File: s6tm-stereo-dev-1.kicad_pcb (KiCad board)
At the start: 4 copper layers, 184 parts, among them J1 Micro_SD_Card_Det1, J2 Conn_01x04_Pin, J3 USB_C_Receptacle_USB2.0_14P, J4 Conn_01x02, J5 AudioJack4, J6 Conn_01x02, J7 Conn_01x02, J8 Conn_01x02, Q1 Q_NMOS, Q2 Q_NMOS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

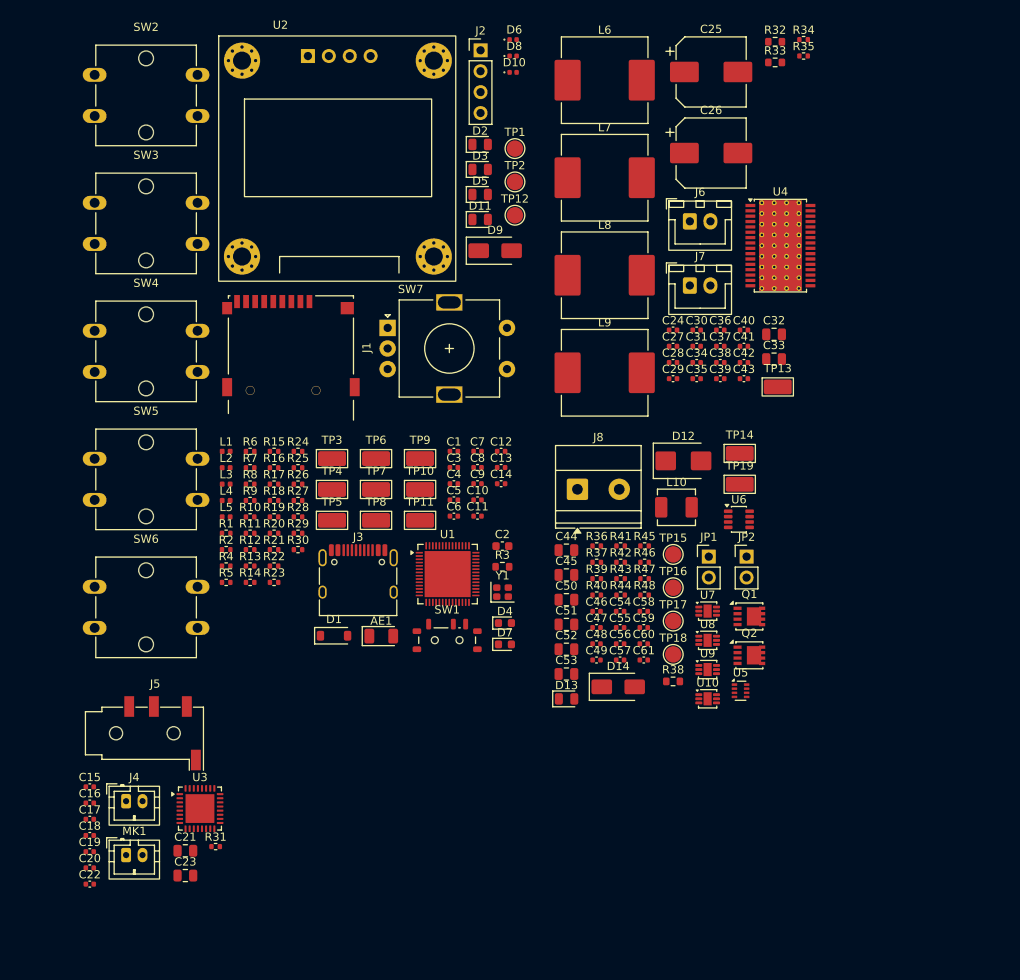
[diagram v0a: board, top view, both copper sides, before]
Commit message: pcb: initial layout
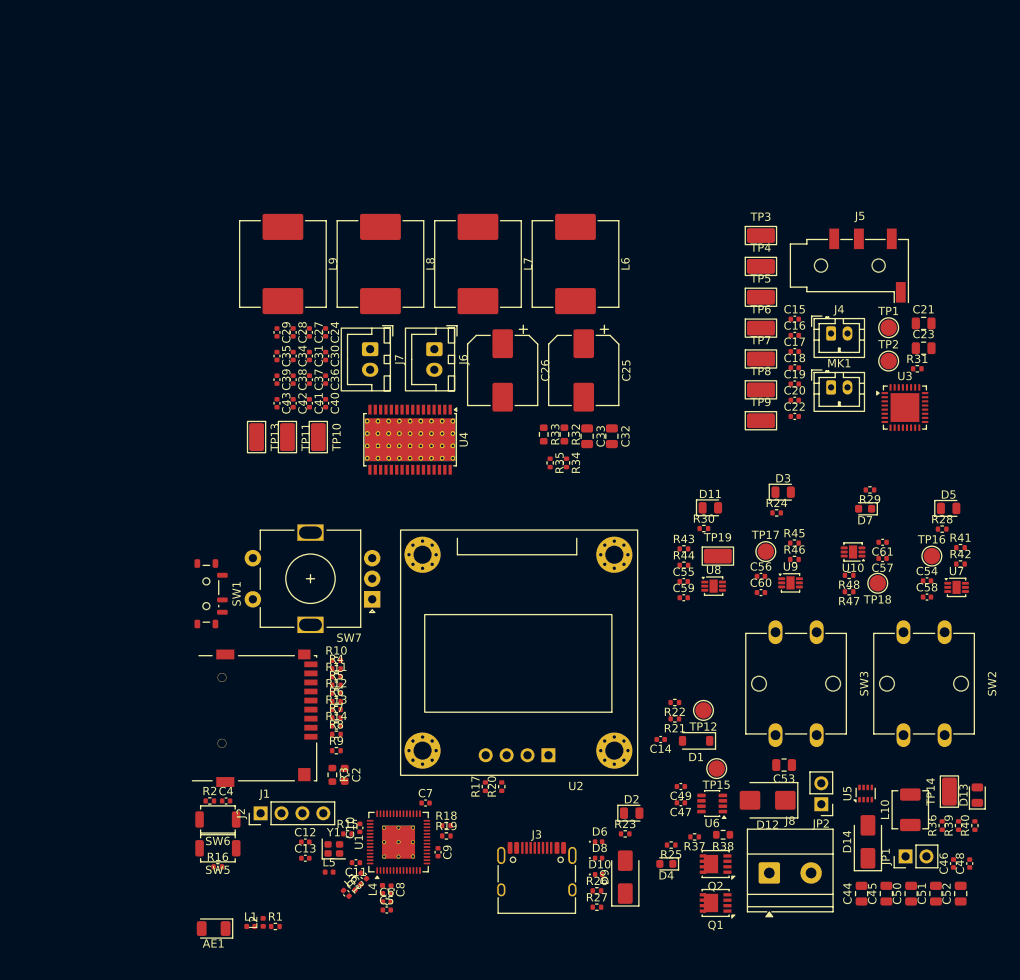
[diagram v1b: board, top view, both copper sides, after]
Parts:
- removed SW4: SW_Push, Button_Switch_THT:SW_SPST_Omron_B3F-40xx
- SW5, SW6: footprint Button_Switch_THT:SW_SPST_Omron_B3F-40xx -> Button_Switch_SMD:SW_SPST_TS-1088-xR020
- U1: footprint Package_DFN_QFN:QFN-56-1EP_7x7mm_P0.4mm_EP5.6x5.6mm -> Package_DFN_QFN:QFN-56-1EP_7x7mm_P0.4mm_EP4x4mm_ThermalVias
- moved SW2 123.5 mm to (134.8, 153.2), turned to -90 degrees
- moved C21 110.2 mm to (132.2, 115.7)
- moved C23 110.2 mm to (132.2, 118.7)
- moved R31 103.1 mm to (131.5, 121.2)
- moved C15 102.8 mm to (116.6, 115.2)
- moved J4 102.8 mm to (121.0, 117.0)
- moved J5 102.8 mm to (124.5, 108.7)
- moved C16 102.8 mm to (116.6, 117.2)
- moved C17 102.8 mm to (116.6, 119.2)
- moved C18 102.8 mm to (116.6, 121.1)
- moved C19 102.8 mm to (116.6, 123.1)
- moved C20 102.8 mm to (116.6, 125.1)
- moved C22 102.8 mm to (116.6, 127.0)
- moved MK1 102.8 mm to (121.0, 123.5)
- moved SW3 102.1 mm to (119.2, 153.2), turned to -90 degrees
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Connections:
- SW5 pad 1: /BOOT -> GND
- SW5 pad 2: GND -> /BOOT
- SW6 pad 1: /CHIP_PU -> GND
- SW6 pad 2: GND -> /CHIP_PU

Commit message: schem: add M3 mounting holes
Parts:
- added H1: MountingHole_Pad, MountingHole:MountingHole_3.2mm_M3_Pad_Via, F.Cu at (25.2, 166.5)
- added H2: MountingHole_Pad, MountingHole:MountingHole_3.2mm_M3_Pad_Via, F.Cu at (25.2, 174.4)
- added H3: MountingHole_Pad, MountingHole:MountingHole_3.2mm_M3_Pad_Via, F.Cu at (25.2, 182.4)
- added H4: MountingHole_Pad, MountingHole:MountingHole_3.2mm_M3_Pad_Via, F.Cu at (25.2, 190.3)

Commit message: schem/pcb: add smt fiducials and tooling holes
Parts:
- added FID1: Fiducial, Fiducial:Fiducial_1mm_Mask2mm, F.Cu at (24.3, 151.8)
- added FID2: Fiducial, Fiducial:Fiducial_1mm_Mask2mm, F.Cu at (24.3, 155.3)
- added FID3: Fiducial, Fiducial:Fiducial_1mm_Mask2mm, F.Cu at (24.3, 158.9)
- added H5: MountingHole, MountingHole:ToolingHole_1.152mm, F.Cu at (27.3, 151.2)
- added H6: MountingHole, MountingHole:ToolingHole_1.152mm, F.Cu at (27.3, 153.7)
- added H7: MountingHole, MountingHole:ToolingHole_1.152mm, F.Cu at (27.3, 156.1)

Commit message: schem/pcb: remove extra mounting hole
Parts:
- removed H4: MountingHole_Pad, MountingHole:MountingHole_3.2mm_M3_Pad_Via
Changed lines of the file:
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@@
 		)
-	)
-	(footprint "MountingHole:MountingHole_3.2mm_M3_Pad_Via"
-		(layer "F.Cu")
-		(at 25.225 190.325)
-		(descr "Mounting Hole 3.2mm, M3, generated by kicad-footprint-generator mountinghole.py")
-		(tags "mountinghole M3")
-		(property "Reference" "H4"
-			(at 0 -4.15 0)
-			(layer "F.SilkS")
-			(effects
-				(font
-					(size 1 1)
-					(thickness 0.15)
-				)
-			)
-		)
-		(property "Value" "MountingHole_Pad"
-			(at 0 4.15 0)
-			(layer "F.Fab")
-			(effects
-				(font
-					(size 1 1)
-					(thickness 0.15)
-				)
-			)
-		)
-		(property "Datasheet" ""
-			(at 0 0 0)
-			(layer "F.Fab")
-			(hide yes)
-			(effects
-				(font
-					(size 1.27 1.27)
-				)
-			)
-		)
-		(property "Description" "Mounting Hole with connection"
-			(at 0 0 0)
-			(layer "F.Fab")
-			(hide yes)
-			(effects
-				(font
-					(size 1.27 1.27)
-				)
-			)
-		)
-		(property "KiLib_Generator" "mounting_hardware/mounting_hole"
-			(at 0 0 0)
-			(layer "F.SilkS")
-			(hide yes)
-			(effects
-				(font
-					(size 1 1)
-					(thickness 0.15)
-				)
-			)
-		)
-		(property ki_fp_filters "MountingHole*Pad*")
-		(sheetname "/")
-		(sheetfile "s6tm-stereo-dev-1.kicad_sch")
-		(units
-			(unit
-				(name "A")
-				(pins "1")
-			)
-		)
-		(attr exclude_from_bom)
-		(duplicate_pad_numbers_are_jumpers no)
-		(fp_circle
-			(center 0 0)
-			(end 3.2 0)
-			(stroke
-				(width 0.15)
-				(type solid)
-			)
-			(fill no)
-			(layer "Cmts.User")
-		)
-		(fp_circle
-			(center 0 0)
-			(end 3.45 0)
-			(stroke
-				(width 0.05)
-				(type solid)
-			)
-			(fill no)
-			(layer "F.CrtYd")
-		)
-		(fp_text user "${REFERENCE}"
-			(at 0 0 0)
-			(layer "F.Fab")
-			(effects
-				(font
-					(size 1 1)
-					(thickness 0.15)
-				)
-			)
-		)
-		(pad "1" thru_hole circle
-			(at -2.4 0)
-			(size 0.8 0.8)
-			(drill 0.5)
-			(layers "*.Cu" "*.Mask")
-			(remove_unused_layers no)
-			(net "GND")
-			(pinfunction "1_1")
-			(pintype "input")
-			(zone_connect 2)
-		)
-		(pad "1" thru_hole circle
-			(at -1.697056 -1.697056)
-			(size 0.8 0.8)
-			(drill 0.5)
-			(layers "*.Cu" "*.Mask")
-			(remove_unused_layers no)
-			(net "GND")
-			(pinfunction "1_1")
-			(pintype "input")
-			(zone_connect 2)
-		)
-		(pad "1" thru_hole circle
-			(at -1.697056 1.697056)
-			(size 0.8 0.8)
-			(drill 0.5)
-			(layers "*.Cu" "*.Mask")
-			(remove_unused_layers no)
-			(net "GND")
-			(pinfunction "1_1")
-			(pintype "input")
-			(zone_connect 2)
-		)
-		(pad "1" thru_hole circle
-			(at 0 -2.4)
-			(size 0.8 0.8)
-			(drill 0.5)
-			(layers "*.Cu" "*.Mask")
-			(remove_unused_layers no)
-			(net "GND")
-			(pinfunction "1_1")
-			(pintype "input")
-			(zone_connect 2)
-		)
-		(pad "1" thru_hole circle
-			(at 0 0)
-			(size 6.4 6.4)
-			(drill 3.2)
-			(layers "*.Cu" "*.Mask")
-			(remove_unused_layers no)
-			(net "GND")
-			(pinfunction "1_1")
-			(pintype "input")
-			(zone_connect 2)
-		)
-		(pad "1" thru_hole circle
-			(at 0 2.4)
-			(size 0.8 0.8)
-			(drill 0.5)
-			(layers "*.Cu" "*.Mask")
-			(remove_unused_layers no)
-			(net "GND")
-			(pinfunction "1_1")
-			(pintype "input")
-			(zone_connect 2)
-		)
-		(pad "1" thru_hole circle
-			(at 1.697056 -1.697056)
-			(size 0.8 0.8)
-			(drill 0.5)
-			(layers "*.Cu" "*.Mask")
-			(remove_unused_layers no)
-			(net "GND")
-			(pinfunction "1_1")
-			(pintype "input")
-			(zone_connect 2)
-		)
-		(pad "1" thru_hole circle
-			(at 1.697056 1.697056)
-			(size 0.8 0.8)
-			(drill 0.5)
-			(layers "*.Cu" "*.Mask")
-			(remove_unused_layers no)
-			(net "GND")
-			(pinfunction "1_1")
-			(pintype "input")
-			(zone_connect 2)
-		)
-		(pad "1" thru_hole circle
-			(at 2.4 0)
-			(size 0.8 0.8)
-			(drill 0.5)
-			(layers "*.Cu" "*.Mask")
-			(remove_unused_layers no)
-			(net "GND")
-			(pinfunction "1_1")
-			(pintype "input")
-			(zone_connect 2)
-		)
-		(embedded_fonts no)
 	)
 	(footprint "Resistor_SMD:R_0402_1005Metric"

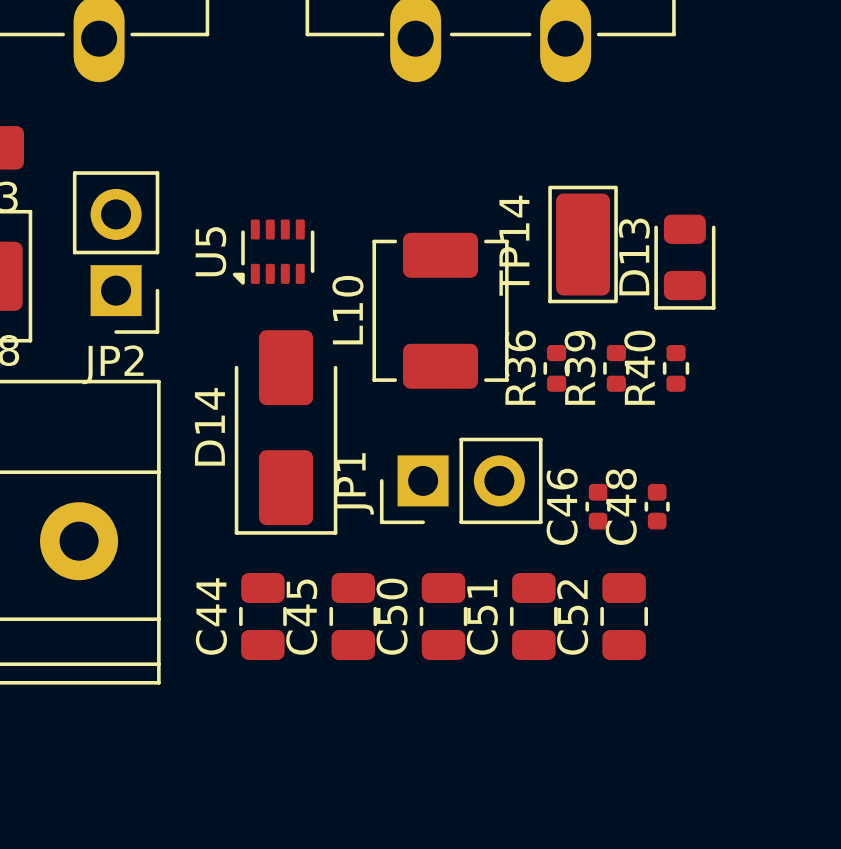
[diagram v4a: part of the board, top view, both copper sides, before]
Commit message: pcb: add smps routing
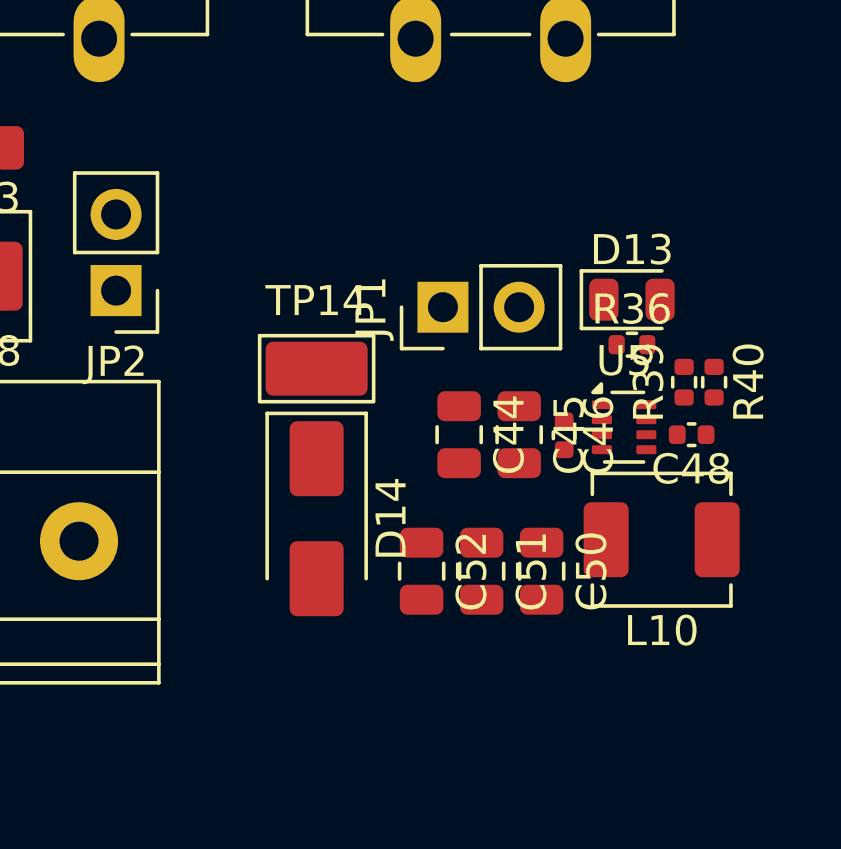
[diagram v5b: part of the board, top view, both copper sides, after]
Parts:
- moved U5 12.9 mm to (136.8, 178.7), turned to 0 degrees
- moved L10 10.6 mm to (138.0, 182.4), turned to 180 degrees
- moved TP14 9.80 mm to (126.5, 176.8), turned to 0 degrees
- moved C44 8.92 mm to (131.2, 178.9), turned to -90 degrees
- moved C45 8.20 mm to (133.2, 178.9), turned to -90 degrees
- moved C52 6.92 mm to (130.0, 183.5), turned to -90 degrees
- moved JP1 5.83 mm to (130.7, 174.7)
- moved C50 3.60 mm to (134.0, 183.5), turned to -90 degrees
- moved D14 3.20 mm to (126.5, 181.8), turned to -90 degrees
- moved C48 2.66 mm to (139.0, 178.9), turned to 180 degrees
- moved C46 2.63 mm to (134.8, 179.0), turned to -90 degrees
- moved R36 2.63 mm to (137.0, 175.9), turned to 0 degrees
- moved R39 2.31 mm to (138.8, 177.2)
- moved C51 2.30 mm to (132.0, 183.5), turned to -90 degrees
- moved D13 2.26 mm to (137.0, 174.4), turned to 0 degrees
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
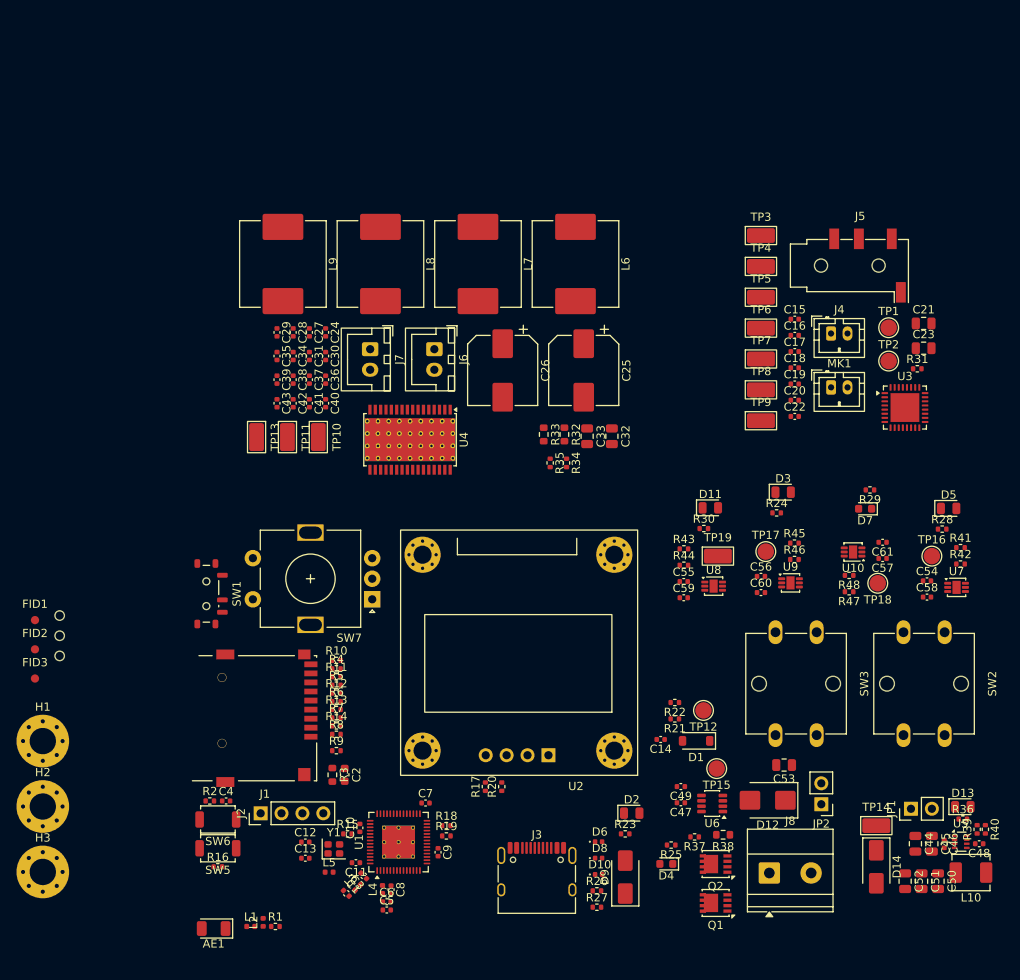
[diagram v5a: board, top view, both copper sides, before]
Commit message: pcb: add LM74502H layout
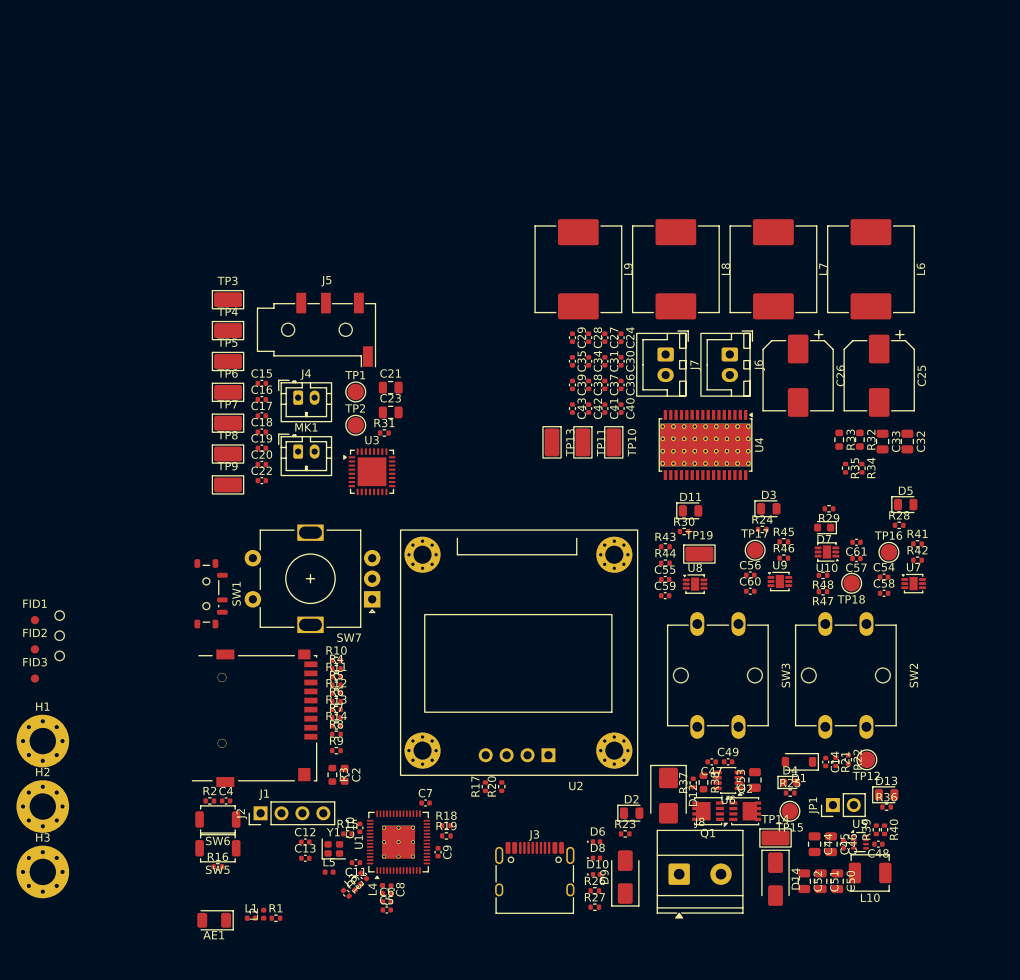
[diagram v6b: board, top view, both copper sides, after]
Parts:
- removed JP2: Jumper_2_Small_Open, Connector_PinHeader_2.54mm:PinHeader_1x02_P2.54mm_Vertical
- moved C15 65.2 mm to (51.8, 123.0)
- moved C16 65.2 mm to (51.8, 125.0)
- moved C17 65.2 mm to (51.8, 127.0)
- moved C18 65.2 mm to (51.8, 128.9)
- moved C19 65.2 mm to (51.8, 130.9)
- moved C20 65.2 mm to (51.8, 132.9)
- moved C21 65.2 mm to (67.5, 123.5)
- moved C22 65.2 mm to (51.8, 134.8)
- moved C23 65.2 mm to (67.5, 126.5)
- moved J4 65.2 mm to (56.2, 124.8)
- moved J5 65.2 mm to (59.8, 116.5)
- moved MK1 65.2 mm to (56.2, 131.3)
- moved TP1 65.2 mm to (63.2, 124.0)
- moved TP2 65.2 mm to (63.2, 128.1)
- moved TP3 65.2 mm to (47.7, 112.8)
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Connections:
- J8 pad 1: GND -> +Vin
- J8 pad 2: +Vin -> GND
- U6 pad 1: Net-(JP2-A) -> +Vin
